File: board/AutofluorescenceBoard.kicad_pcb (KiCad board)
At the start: 2 copper layers, 76.2 x 76.2 mm, 45 parts, among them J1 2002411212, Q1 BSS138, U1 PAM2863ECR, U2 PAM2863ECR, U3 PAM2863ECR

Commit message: Wizard
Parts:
- removed 365nm: 365nm, AutofluorescenceBoard:365nm
- removed 405nm: 405nm, AutofluorescenceBoard:405nm
- removed 490nm: 490nm, AutofluorescenceBoard:490nm
- removed D5: MMSZ5240BT1G, MRDT_Devices:SOD-123_ONS-L
- removed G*** (x3): LOGO, LOGO
- removed MOSFET1: TPC8132_LQS, MRDT_Devices:SOP-8_TOS-L
- removed WhiteLED: LED, AutofluorescenceBoard:INS63AT5UW
- added D1: 365nm, AutofluorescenceBoard:365nm, F.Cu at (161.8, 101.5)
- added D2: 405nm, AutofluorescenceBoard:405nm, F.Cu at (160.5, 109.9)
- added D3: 490nm, AutofluorescenceBoard:490nm, F.Cu at (165.9, 111.5)
- added D6: LED, AutofluorescenceBoard:INS63AT5UW, F.Cu at (146.5, 109.2)
- moved H3 94.7 mm to (124.8, 97.7), turned to 0 degrees
- moved H1 83.0 mm to (124.8, 77.3)
- moved FanConn1 79.2 mm to (137.6, 109.1), turned to 0 degrees
- moved Q1 67.0 mm to (126.5, 111.1), turned to 0 degrees
- moved R3 64.6 mm to (142.3, 92.0)
- moved Conn1 61.1 mm to (153.0, 95.1), turned to 0 degrees
- moved R9 57.7 mm to (131.2, 110.2)
- moved J1 56.6 mm to (139.6, 103.4)
- moved U2 52.6 mm to (162.2, 77.8)
- moved TP2 52.0 mm to (168.2, 73.1)
- moved R2 52.0 mm to (142.3, 82.3), turned to 0 degrees
- moved L1 51.4 mm to (153.9, 71.6), turned to 0 degrees
- moved L2 49.0 mm to (153.9, 79.1), turned to 0 degrees
- moved TP3 49.0 mm to (168.2, 76.7), turned to 0 degrees
- moved H4 48.1 mm to (124.8, 107.9)
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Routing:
- net +12V: track 186.9 -> 0.00 mm
- net ISET 365nm: track 82.8 -> 0.00 mm
- net ISET 405nm: track 67.5 -> 0.00 mm
- net ISET 490nm: track 45.6 -> 0.00 mm
- net Net-(J1-Pad2): track 33.7 -> 0.00 mm
- net Net-(U1-ISENSE): track 26.5 -> 0.00 mm
- net Net-(U2-ISENSE): track 23.4 -> 0.00 mm
- net Net-(U3-ISENSE): track 20.7 -> 0.00 mm
- net White LED: track 19.1 -> 0.00 mm
- net Net-(D1-Pad1): track 17.4 -> 0.00 mm
- net Net-(CR1-Pad2): track 13.7 -> 0.00 mm
- net Net-(CR2-Pad2): track 13.5 -> 0.00 mm
- net Net-(D2-Pad2): track 12.0 -> 0.00 mm
- net Net-(CR3-Pad2): track 12.0 -> 0.00 mm
- net Net-(D1-Pad2): track 6.57 -> 0.00 mm
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- removed copper zone on F.Cu, net GND
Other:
- board outline removed
- board text removed: "Mars Rover Design Team Autofluorescense Board 2026 Rev1"

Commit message: Rev2 Initial Component Placement
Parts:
- removed TP1, TP2, TP3: TestPoint, TestPoint:TestPoint_Pad_D1.5mm
- added MOSFET1: TPC8132_LQS, AutofluorescenceBoard:SOP-8_TOS-M, F.Cu at (146.5, 81.4)
- added R10: 10K, Resistor_SMD:R_0603_1608Metric_Pad0.98x0.95mm_HandSolder, F.Cu at (135.0, 79.2)
- D1, D2, D3, D6: moved to B.Cu
- H1, H2, H3, H4: footprint MRDT_Drill_Holes:6_32_Hole_Corner -> MountingHole:MountingHole_2.2mm_M2
- moved F2 44.3 mm to (124.5, 87.4), turned to 180 degrees
- moved R5 44.3 mm to (124.5, 90.8), turned to 90 degrees
- moved H2 41.5 mm to (164.1, 74.2)
- moved FanConn1 41.1 mm to (156.5, 72.6)
- moved H4 39.6 mm to (164.1, 113.3)
- moved U3 35.6 mm to (138.7, 111.3), turned to 90 degrees
- moved D4 34.0 mm to (139.1, 79.2)
- moved U2 33.6 mm to (130.7, 89.5)
- moved L3 33.2 mm to (132.1, 111.8), turned to 90 degrees
- moved C2 33.2 mm to (136.1, 88.4), turned to 90 degrees
- moved C3 32.4 mm to (142.7, 105.2), turned to -90 degrees
- moved L1 31.0 mm to (161.5, 101.6)
- moved R8 30.9 mm to (157.5, 80.3), turned to 90 degrees
- moved J1 30.6 mm to (147.9, 74.0)
- moved Conn1 30.3 mm to (131.1, 74.2)
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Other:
- board outline added: 44.5 x 44.4 mm
- copper layers 2 -> 4

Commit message: Fixed Errror
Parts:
- added H2: MountingHole, MountingHole:MountingHole_2.2mm_M2, F.Cu at (2.48, 2.48)
- added H3: MountingHole, MountingHole:MountingHole_2.2mm_M2, F.Cu at (2.48, 8.43)
- added H4: MountingHole, MountingHole:MountingHole_2.2mm_M2, F.Cu at (2.48, 14.4)
- U1, U2, U3: footprint AutofluorescenceBoard:SOIC_863ECR_DIO -> PAM2863ECR:SOIC_863ECR_DIO

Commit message: Fixed Footprint for Zener Diode
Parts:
- added D5: MMSZ5240BT1G, AutofluorescenceBoard:DIO_MMSZ5221BT1G, F.Cu at (162.4, 80.3)
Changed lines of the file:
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@@
 		)
+	)
+	(footprint "AutofluorescenceBoard:DIO_MMSZ5221BT1G"
+		(layer "F.Cu")
+		(at 162.449 80.264)
+		(property "Reference" "D5"
+			(at 0.635 -1.905 0)
+			(layer "F.SilkS")
+			(effects
+				(font
+					(size 1 1)
+					(thickness 0.15)
+				)
+			)
+		)
+		(property "Value" "MMSZ5240BT1G"
+			(at 7.62 1.905 0)
+			(layer "F.Fab")
+			(effects
+				(font
+					(size 1 1)
+					(thickness 0.15)
+				)
+			)
+		)
+		(property "Datasheet" "https://www.onsemi.com/pdf/datasheet/mmsz5221bt1-d.pdf"
+			(at 0 0 0)
+			(layer "F.Fab")
+			(hide yes)
+			(effects
+				(font
+					(size 1.27 1.27)
+					(thickness 0.15)
+				)
+			)
+		)
+		(property "Description" ""
+			(at 0 0 0)
+			(layer "F.Fab")
+			(hide yes)
+			(effects
+				(font
+					(size 1.27 1.27)
+					(thickness 0.15)
+				)
+			)
+		)
+		(property ki_fp_filters "SOD-123_ONS SOD-123_ONS-M SOD-123_ONS-L")
+		(sheetname "/")
+		(sheetfile "AutofluorescenceBoard.kicad_sch")
+		(attr smd)
+		(fp_line
+			(start -0.86 -0.8)
+			(end 0.86 -0.8)
+			(stroke
+				(width 0.127)
+				(type solid)
+			)
+			(layer "F.SilkS")
+		)
+		(fp_line
+			(start -0.86 0.8)
+			(end 0.86 0.8)
+			(stroke
+				(width 0.127)
+				(type solid)
+			)
+			(layer "F.SilkS")
+		)
+		(fp_circle
+			(center -2.6 0)
+			(end -2.5 0)
+			(stroke
+				(width 0.2)
+				(type solid)
+			)
+			(fill no)
+			(layer "F.SilkS")
+		)
+		(fp_line
+			(start -2.34 -1.05)
+			(end 2.34 -1.05)
+			(stroke
+				(width 0.05)
+				(type solid)
+			)
+			(layer "F.CrtYd")
+		)
+		(fp_line
+			(start -2.34 1.05)
+			(end -2.34 -1.05)
+			(stroke
+				(width 0.05)
+				(type solid)
+			)
+			(layer "F.CrtYd")
+		)
+		(fp_line
+			(start 2.34 -1.05)
+			(end 2.34 1.05)
+			(stroke
+				(width 0.05)
+				(type solid)
+			)
+			(layer "F.CrtYd")
+		)
+		(fp_line
+			(start 2.34 1.05)
+			(end -2.34 1.05)
+			(stroke
+				(width 0.05)
+				(type solid)
+			)
+			(layer "F.CrtYd")
+		)
+		(fp_line
+			(start -1.345 -0.8)
+			(end -1.345 0.8)
+			(stroke
+				(width 0.127)
+				(type solid)
+			)
+			(layer "F.Fab")
+		)
+		(fp_line
+			(start -1.345 0.8)
+			(end 1.345 0.8)
+			(stroke
+				(width 0.127)
+				(type solid)
+			)
+			(layer "F.Fab")
+		)
+		(fp_line
+			(start 1.345 -0.8)
+			(end -1.345 -0.8)
+			(stroke
+				(width 0.127)
+				(type solid)
+			)
+			(layer "F.Fab")
+		)
+		(fp_line
+			(start 1.345 0.8)
+			(end 1.345 -0.8)
+			(stroke
+				(width 0.127)
+				(type solid)
+			)
+			(layer "F.Fab")
+		)
+		(fp_circle
+			(center -2.6 0)
+			(end -2.5 0)
+			(stroke
+				(width 0.2)
+				(type solid)
+			)
+			(fill no)
+			(layer "F.Fab")
+		)
+		(pad "1" smd rect
+			(at -1.635 0)
+			(size 0.91 1.22)
+			(layers "F.Cu" "F.Mask" "F.Paste")
+			(net 2 "+12V")
+			(pintype "unspecified")
+			(solder_mask_margin 0.102)
+		)
+		(pad "2" smd rect
+			(at 1.635 0)
+			(size 0.91 1.22)
+			(layers "F.Cu" "F.Mask" "F.Paste")
+			(net 19 "Net-(MOSFET1-GATE)")
+			(pintype "unspecified")
+			(solder_mask_margin 0.102)
+		)
+		(embedded_fonts no)
 	)
 	(footprint "Fuse:Fuse_0603_1608Metric"

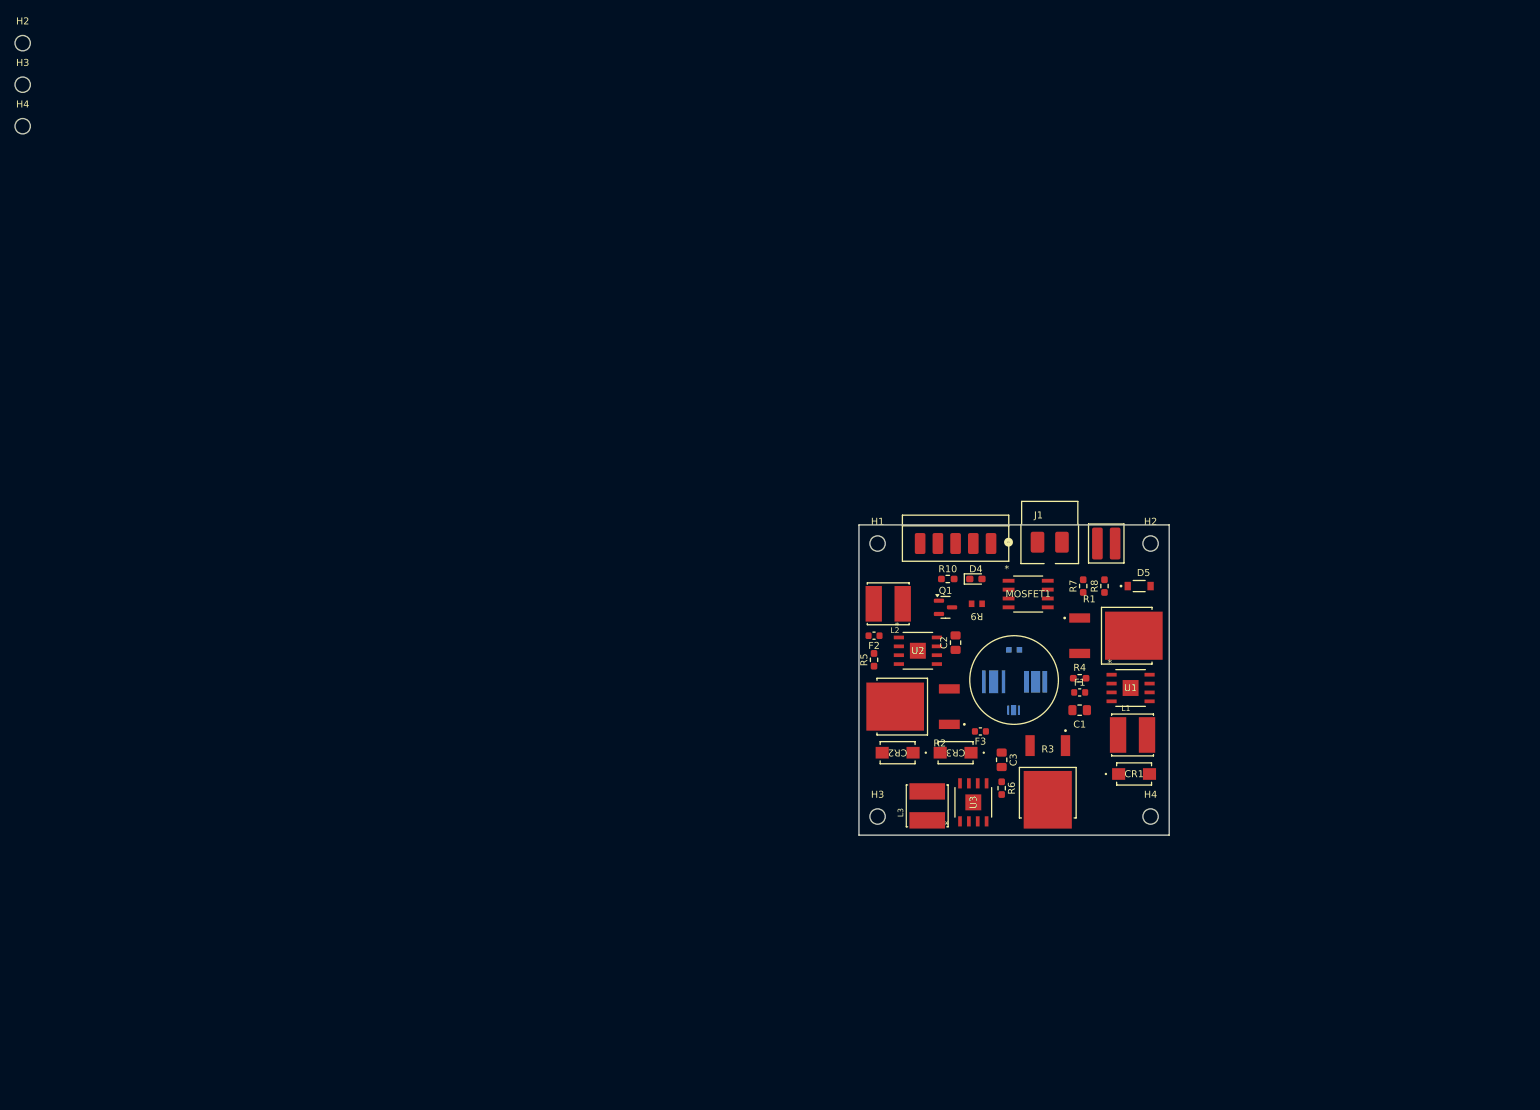
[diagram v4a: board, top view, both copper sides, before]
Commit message: Added some traces and update some footprints
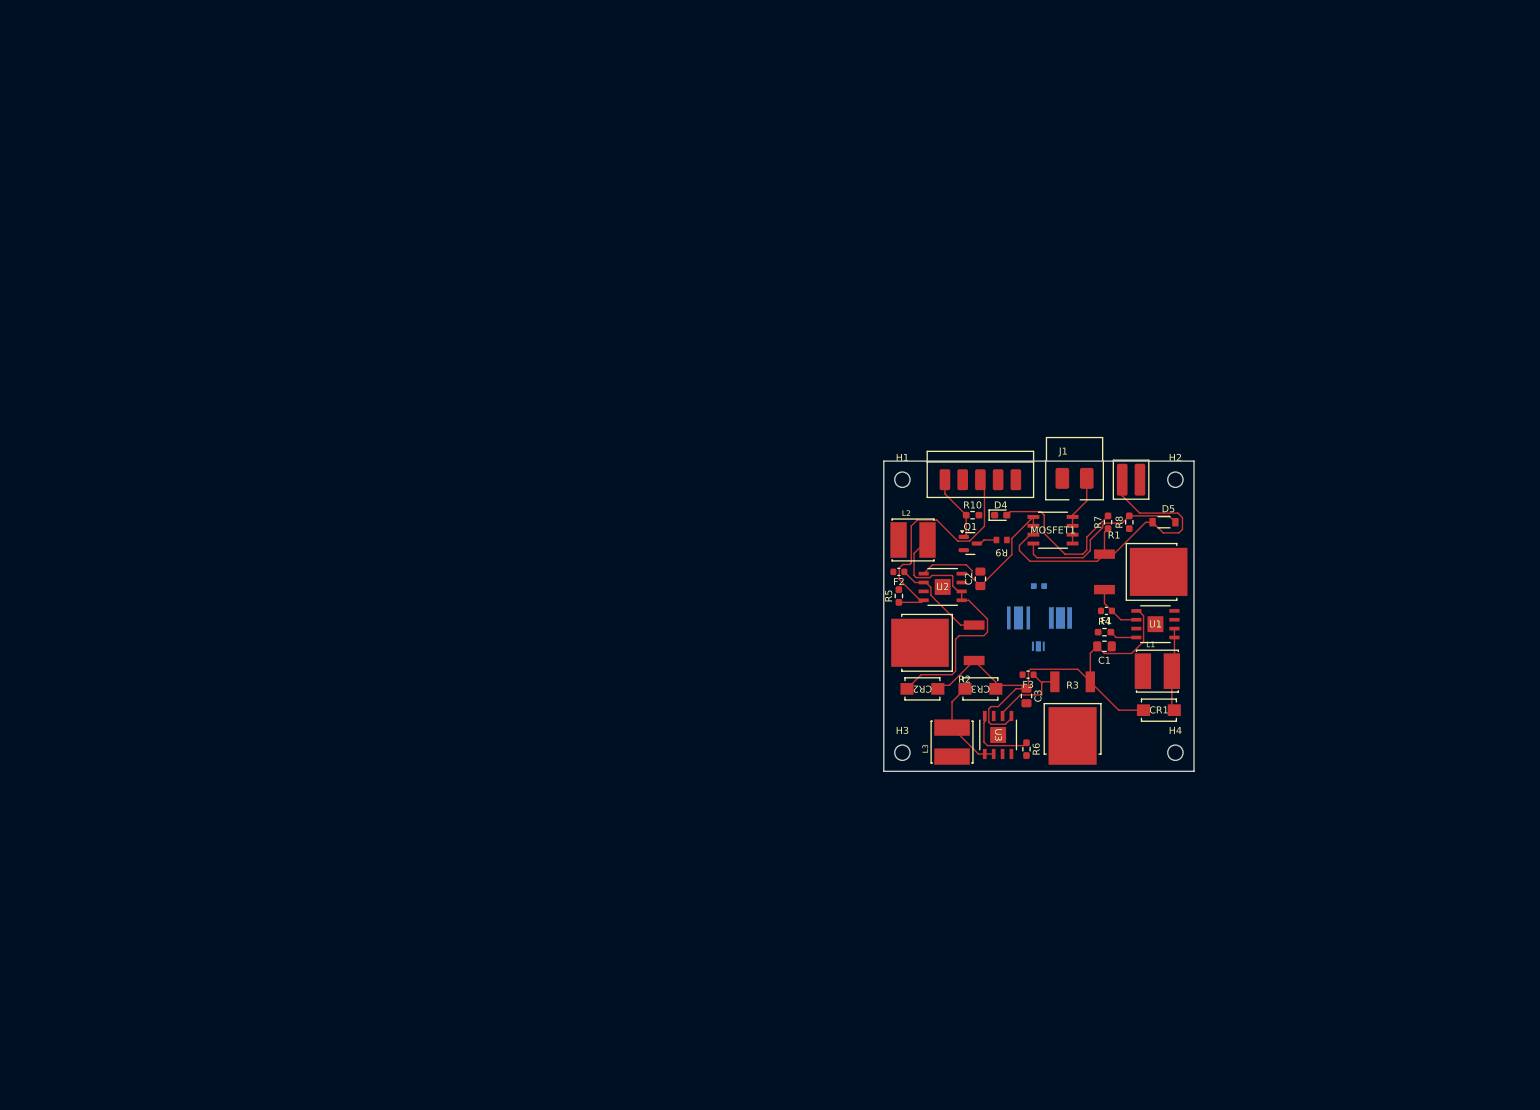
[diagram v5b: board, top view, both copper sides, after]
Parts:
- removed the H2 at (2.48, 2.48)
- removed the H3 at (2.48, 8.43)
- removed the H4 at (2.48, 14.4)
- moved F1 12.3 mm to (157.8, 83.8), turned to 180 degrees
- moved F3 10.6 mm to (146.5, 93.0)
- moved U3 10.3 mm to (142.2, 101.6), turned to -90 degrees
- moved C3 9.81 mm to (146.3, 96.0)
- moved CR1 9.81 mm to (165.3, 98.0)
- moved CR2 9.81 mm to (131.4, 95.0)
- moved Conn1 9.81 mm to (134.6, 65.0)
- moved D4 9.81 mm to (142.6, 70.1)
- moved FanConn1 9.81 mm to (160.0, 63.5)
- moved J1 9.81 mm to (151.4, 64.8)
- moved R1 9.81 mm to (162.7, 78.2)
- moved R10 9.81 mm to (138.6, 70.1)
- moved R2 9.81 mm to (133.6, 88.4)
- moved U1 9.81 mm to (164.8, 85.7)
- moved F2 9.81 mm to (128.0, 78.2)
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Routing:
- net +12V: track 0.00 -> 143.9 mm
- net Net-(CR2-Pad2): track 0.00 -> 40.3 mm
- net ISET 405nm: track 0.00 -> 37.3 mm
- net Net-(MOSFET1-GATE): track 0.00 -> 26.0 mm
- net Net-(D4-A): track 0.00 -> 22.1 mm
- net Net-(CR3-Pad2): track 0.00 -> 13.8 mm
- net Net-(U2-ISENSE): track 0.00 -> 13.8 mm
- net Net-(U3-ISENSE): track 0.00 -> 12.5 mm
- net Net-(CR1-Pad2): track 0.00 -> 12.0 mm
- net ISET 490nm: track 0.00 -> 10.3 mm
- net Net-(J1-Pad2): track 0.00 -> 10.2 mm
- net White LED: track 0.00 -> 9.60 mm
- net Net-(U1-ISENSE): track 0.00 -> 7.52 mm
- net ISET 365nm: track 0.00 -> 3.98 mm
- net Net-(Q1-D): track 0.00 -> 3.02 mm
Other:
- board size 44.5 x 44.4 mm -> 44.4 x 44.5 mm

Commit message: Added Planes
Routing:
- added copper zone on F.Cu, net +12V
- added copper zone on B.Cu, net GND
- added copper zone on In1.Cu, net GND
- added copper zone on In2.Cu, net GND
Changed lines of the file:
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@@
 		(net 23)
+	)
+	(zone
+		(net 2)
+		(net_name "+12V")
+		(layer "F.Cu")
+		(hatch edge 0.5)
+		(connect_pads yes
+			(clearance 0.254)
+		)
+		(min_thickness 0.25)
+		(filled_areas_thickness no)
+		(fill yes
+			(thermal_gap 0.5)
+			(thermal_bridge_width 0.5)
+		)
+		(polygon
+			(pts
+				(xy 125.476 61.976) (xy 170.688 61.976) (xy 170.688 107.188) (xy 125.476 107.188)
+			)
+		)
+	)
+	(zone
+		(net 1)
+		(net_name "GND")
+		(layer "B.Cu")
+		(hatch edge 0.5)
+		(connect_pads yes
+			(clearance 0.254)
+		)
+		(min_thickness 0.25)
+		(filled_areas_thickness no)
+		(fill yes
+			(thermal_gap 0.5)
+			(thermal_bridge_width 0.5)
+		)
+		(polygon
+			(pts
+				(xy 125.476 61.976) (xy 170.688 61.976) (xy 170.688 107.188) (xy 125.476 107.188)
+			)
+		)
+	)
+	(zone
+		(net 1)
+		(net_name "GND")
+		(layer "In1.Cu")
+		(hatch edge 0.5)
+		(connect_pads yes
+			(clearance 0.254)
+		)
+		(min_thickness 0.25)
+		(filled_areas_thickness no)
+		(fill yes
+			(thermal_gap 0.5)
+			(thermal_bridge_width 0.5)
+		)
+		(polygon
+			(pts
+				(xy 125.476 61.976) (xy 170.688 61.976) (xy 170.688 107.188) (xy 125.476 107.188)
+			)
+		)
+	)
+	(zone
+		(net 1)
+		(net_name "GND")
+		(layer "In2.Cu")
+		(hatch edge 0.5)
+		(connect_pads yes
+			(clearance 0.254)
+		)
+		(min_thickness 0.25)
+		(filled_areas_thickness no)
+		(fill yes
+			(thermal_gap 0.5)
+			(thermal_bridge_width 0.5)
+		)
+		(polygon
+			(pts
+				(xy 125.581998 61.976) (xy 170.793998 61.976) (xy 170.793998 107.188) (xy 125.581998 107.188)
+			)
+		)
 	)
 	(embedded_fonts no)

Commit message: Layout?
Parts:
- moved F2 7.70 mm to (135.5, 76.6), turned to 0 degrees
- moved FanConn1 0.51 mm to (160.0, 64.0)
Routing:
- net +12V: track 143.9 -> 0.00 mm, vias 0 -> 19
- net ISET 490nm: track 10.3 -> 87.4 mm, vias 0 -> 3
- net ISET 365nm: track 3.98 -> 36.3 mm, vias 0 -> 3
- net Net-(D3-Pad1): track 0.00 -> 28.8 mm, vias 0 -> 2
- net Net-(D2-Pad1): track 0.00 -> 23.8 mm, vias 0 -> 2
- net Net-(D1-Pad1): track 0.00 -> 15.0 mm, vias 0 -> 2
- net ISET 405nm: track 37.3 -> 50.7 mm, vias 0 -> 3
- net Net-(D2-Pad2): track 0.00 -> 12.0 mm, vias 0 -> 2
- net Net-(D6-K): track 0.00 -> 8.82 mm, vias 0 -> 2
- net Net-(D1-Pad2): track 0.00 -> 7.53 mm, vias 0 -> 2
- net Net-(CR2-Pad2): track 40.3 -> 47.0 mm, vias 0 -> 4
- net Net-(D3-Pad2): track 0.00 -> 5.22 mm, vias 0 -> 2
- net Net-(U2-ISENSE): track 13.8 -> 15.4 mm, vias 0 -> 3
- net Net-(MOSFET1-GATE): track 26.0 -> 24.7 mm, vias 0 -> 3
- net Net-(U3-ISENSE): track 12.5 -> 11.2 mm, vias 0 -> 3
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- added copper zone on In1.Cu, net +12V
- added copper zone on F.Cu, net GND
- removed copper zone on F.Cu, net +12V
- removed copper zone on In1.Cu, net GND
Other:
- outline, holes or cut-outs redrawn
